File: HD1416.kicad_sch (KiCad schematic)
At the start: 37 parts, among them J1 AudioJack2, Q1 MPSA20, Q2 MPSA20, Q3 BC547A, SW1 SW_SPST

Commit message: minor updates
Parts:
- R1: value (none) -> 10k; footprint (none) -> footprints:CFM12JT10K0
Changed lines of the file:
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@@
       (effects (font (size 1.27 1.27)) (justify left))
     )
-    (property "Value" "" (id 1) (at 95.25 88.8999 0)
+    (property "Value" "10k" (id 1) (at 95.25 88.8999 0)
       (effects (font (size 1.27 1.27)) (justify left))
     )
-    (property "Footprint" "" (id 2) (at 92.71 87.63 0)
+    (property "Footprint" "footprints:CFM12JT10K0" (id 2) (at 92.71 87.63 0)
       (effects (font (size 1.27 1.27)) hide)
     )

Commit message: updates to kicad 8.0
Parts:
- removed H10: A, Connector_Wire:SolderWire-0.5sqmm_1x01_D0.9mm_OD2.3mm, symbol Mechanical:MountingHole_Pad
- removed H11: GND, Connector_Wire:SolderWire-0.5sqmm_1x01_D0.9mm_OD2.3mm, symbol Mechanical:MountingHole_Pad
- C1: Spice_Model .01u -> (none); Spice_Netlist_Enabled Y -> (none); Spice_Primitive C -> (none)
- D1: Spice_Lib_File standard.dio -> (none); Spice_Model D1N4005 -> (none); Spice_Netlist_Enabled Y -> (none); Spice_Primitive D -> (none)
- H3: value 8200 -> "8200"; symbol Mechanical:MountingHole_Pad -> Connector:Conn_01x01_Socket; Spice_Netlist_Enabled N -> (none); Spice_Primitive R -> (none)
- H4: value F -> "E"; symbol Mechanical:MountingHole_Pad -> Connector:Conn_01x01_Socket; Spice_Netlist_Enabled N -> (none); Spice_Primitive R -> (none)
- H5: value E -> "E"; symbol Mechanical:MountingHole_Pad -> Connector:Conn_01x01_Socket; Spice_Netlist_Enabled N -> (none); Spice_Primitive R -> (none)
- H6: value D -> "D"; symbol Mechanical:MountingHole_Pad -> Connector:Conn_01x01_Socket; Spice_Netlist_Enabled N -> (none); Spice_Primitive R -> (none)
- H7: value C -> "C"; symbol Mechanical:MountingHole_Pad -> Connector:Conn_01x01_Socket; Spice_Netlist_Enabled N -> (none); Spice_Primitive R -> (none)
- H8: value B -> "B"; symbol Mechanical:MountingHole_Pad -> Connector:Conn_01x01_Socket; Spice_Netlist_Enabled N -> (none); Spice_Primitive R -> (none)
- J1: Spice_Model 1 -> (none); Spice_Netlist_Enabled Y -> (none); Spice_Primitive R -> (none)
- J2: renamed from H9; symbol Mechanical:MountingHole_Pad -> Connector:Conn_01x01_Socket; Spice_Netlist_Enabled N -> (none); Spice_Primitive R -> (none)
- LS1: Spice_Model 50 -> (none); Spice_Netlist_Enabled Y -> (none); Spice_Primitive R -> (none)
- Q1, Q2: Spice_Lib_File standard.bjt -> (none); Spice_Model MPSA20 -> (none); Spice_Netlist_Enabled Y -> (none); Spice_Node_Sequence 3 2 1 -> (none); Spice_Primitive Q -> (none)
- Q3: Spice_Lib_File standard.bjt -> (none); Spice_Model BC547A -> (none); Spice_Netlist_Enabled Y -> (none); Spice_Node_Sequence 3 2 1 -> (none); Spice_Primitive Q -> (none)
- R3: Spice_Lib_File Pot2.lib -> (none); Spice_Model pot_lin2 -> (none); Spice_Netlist_Enabled Y -> (none); Spice_Primitive X -> (none)
- R8: Spice_Lib_File Pot.lib -> (none); Spice_Model pot_lin -> (none); Spice_Netlist_Enabled Y -> (none); Spice_Primitive X -> (none)
- SW1: value SW_SPST -> ${SIM.PARAMS}; footprint (none) -> Connector_Wire:SolderWire-0.75sqmm_1x02_P4.8mm_D1.25mm_OD2.3mm; Spice_Netlist_Enabled N -> (none); Spice_Primitive R -> (none)
- TP1: value 2.4 -> "2.4"; Spice_Netlist_Enabled N -> (none); Spice_Primitive R -> (none)
- TP2: value -0.3 -> "-0.3"; Spice_Netlist_Enabled N -> (none); Spice_Primitive R -> (none)
- TP3: value -2.1 -> "-2.1"; Spice_Netlist_Enabled N -> (none); Spice_Primitive R -> (none)
- TP4: value 5.1 -> "5.1"; Spice_Netlist_Enabled N -> (none); Spice_Primitive R -> (none)
- TP5: value 0.5 -> "0.5"; Spice_Netlist_Enabled N -> (none); Spice_Primitive R -> (none)
- TP6: value 7.5 -> "7.5"; Spice_Netlist_Enabled N -> (none); Spice_Primitive R -> (none)
- V1: symbol pspice:VSOURCE -> Simulation_SPICE:VDC; Spice_Model dc 9 -> (none); Spice_Netlist_Enabled Y -> (none); Spice_Primitive V -> (none)
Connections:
- net GND: now also C1.1
- net at C5.1, H4.1 (Pin_1), H5.1 (Pin_1)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: no longer H3.1, J1.S, R9.2
- net at C1.2, J2.1 (Pin_1), SW1.1 (A): now also D1.2 (A)
- new net: H3.1 (Pin_1), J1.S, R9.2
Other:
- moved on the sheet: C1, R9, SW1

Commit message: updates to schematic
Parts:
- H5: value "E" -> "F"
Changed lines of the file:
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@@
 		(at 214.63 139.7 180)
 		(unit 1)
-		(exclude_from_sim no)
+		(exclude_from_sim yes)
 		(in_bom yes)
 		(on_board yes)
@@
 			)
 		)
-		(property "Value" "\"E\""
+		(property "Value" "\"F\""
 			(at 218.44 140.97 0)
 			(effects
@@
 		(at 187.96 143.51 180)
 		(unit 1)
-		(exclude_from_sim no)
+		(exclude_from_sim yes)
 		(in_bom yes)
 		(on_board yes)
@@
 		(at 227.33 147.32 0)
 		(unit 1)
-		(exclude_from_sim no)
+		(exclude_from_sim yes)
 		(in_bom yes)
 		(on_board yes)
@@
 		(at 205.74 147.32 0)
 		(unit 1)
-		(exclude_from_sim no)
+		(exclude_from_sim yes)
 		(in_bom yes)
 		(on_board yes)
@@
 		(at 210.82 147.32 270)
 		(unit 1)
-		(exclude_from_sim no)
+		(exclude_from_sim yes)
 		(in_bom yes)
 		(on_board yes)
@@
 		(at 199.39 123.19 90)
 		(unit 1)
-		(exclude_from_sim no)
-		(in_bom yes)
-		(on_board yes)
+		(exclude_from_sim yes)
+		(in_bom yes)
+		(on_board yes)

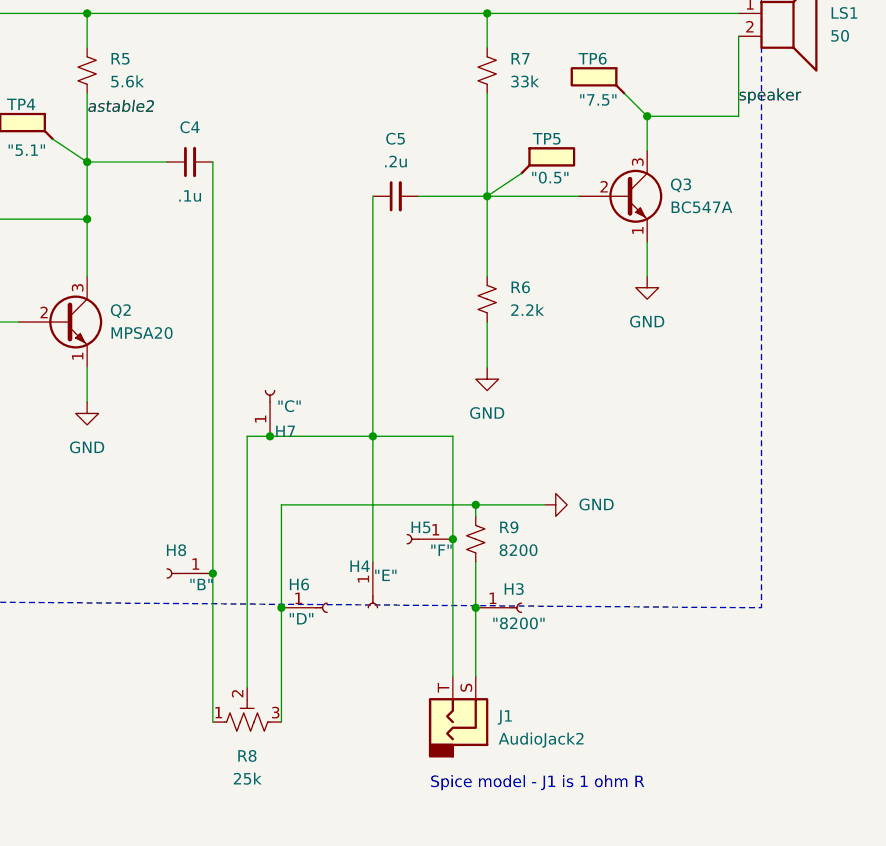
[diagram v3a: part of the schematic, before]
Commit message: updates to audio jack
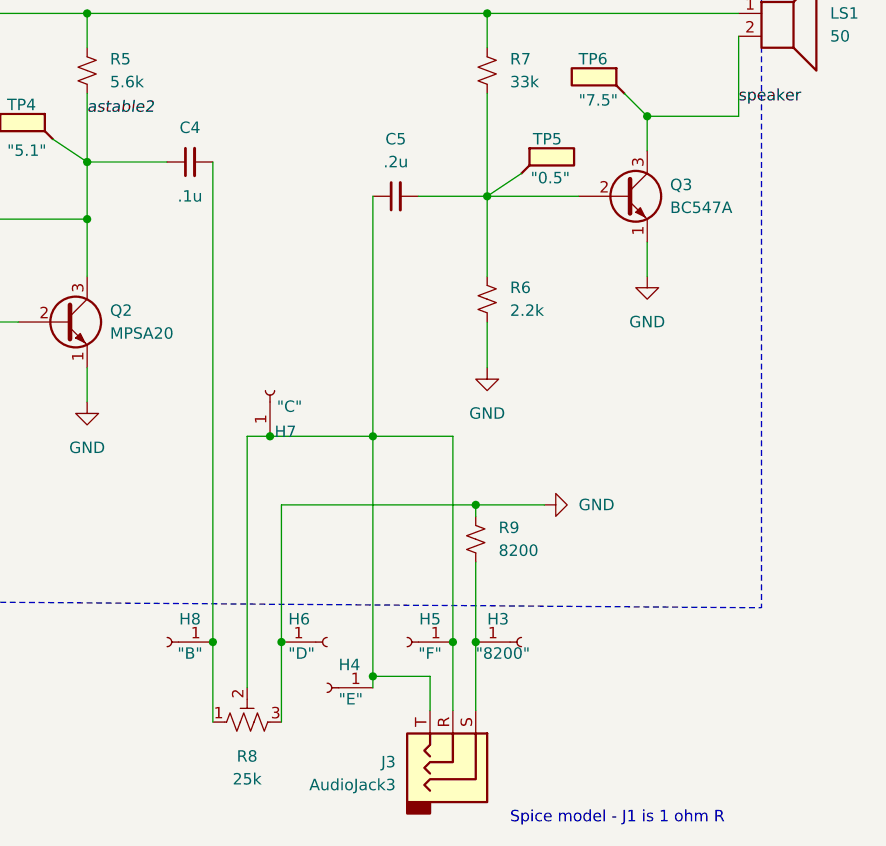
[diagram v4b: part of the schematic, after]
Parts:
- removed J1: AudioJack2, Connector_Wire:SolderWire-0.5sqmm_1x02_P4.8mm_D0.9mm_OD2.3mm, symbol Connector:AudioJack2
- added J3: AudioJack3, symbol Connector_Audio:AudioJack3
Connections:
- net at C5.1, H4.1 (Pin_1), H5.1 (Pin_1)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: now also J3.R, J3.T
- net at H3.1 (Pin_1), R9.2: now also J3.S
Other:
- moved on the sheet: H3, H4, H5, H6, H8
